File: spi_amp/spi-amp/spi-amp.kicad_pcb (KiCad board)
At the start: 4 copper layers, 5 parts, among them J1 IN+, J2 IN-, J3 OUT+, J4 OUT-, U1 LMH6401

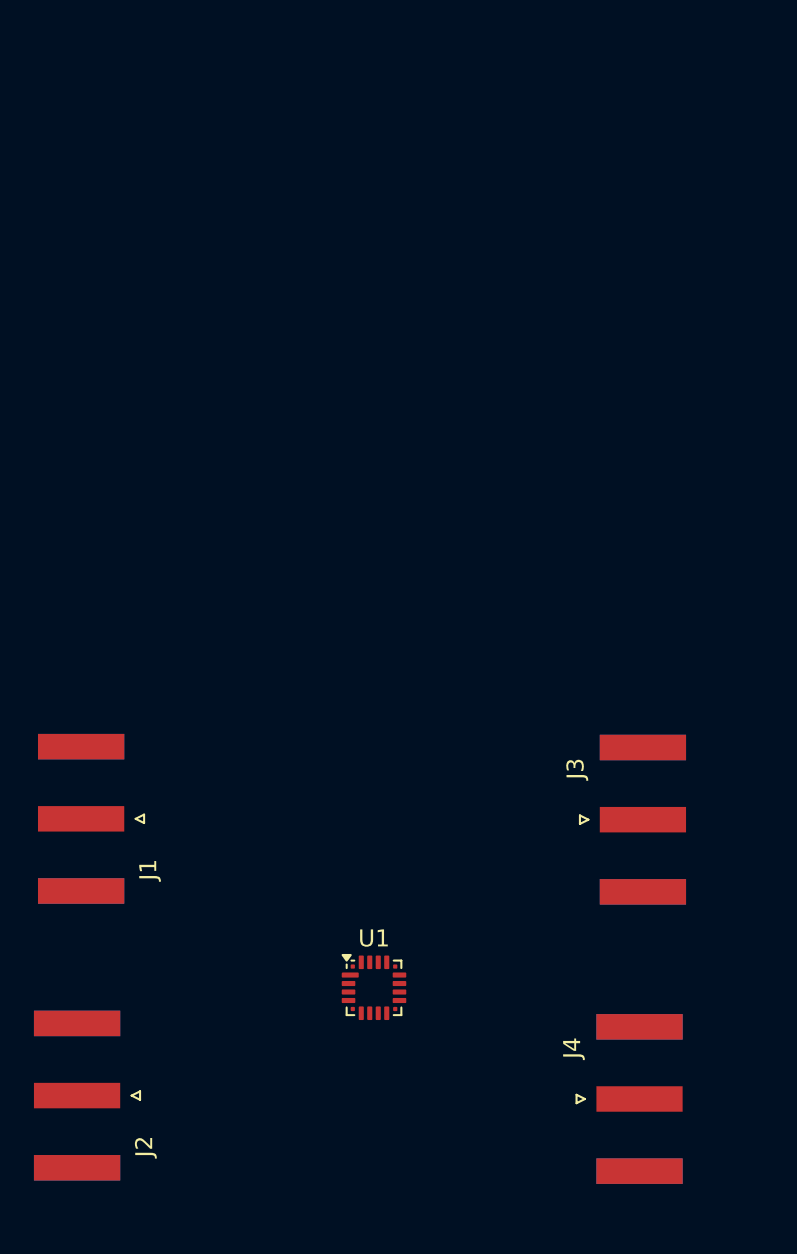
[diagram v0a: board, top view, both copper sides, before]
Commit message: Added SMA connectors with the correct distances.
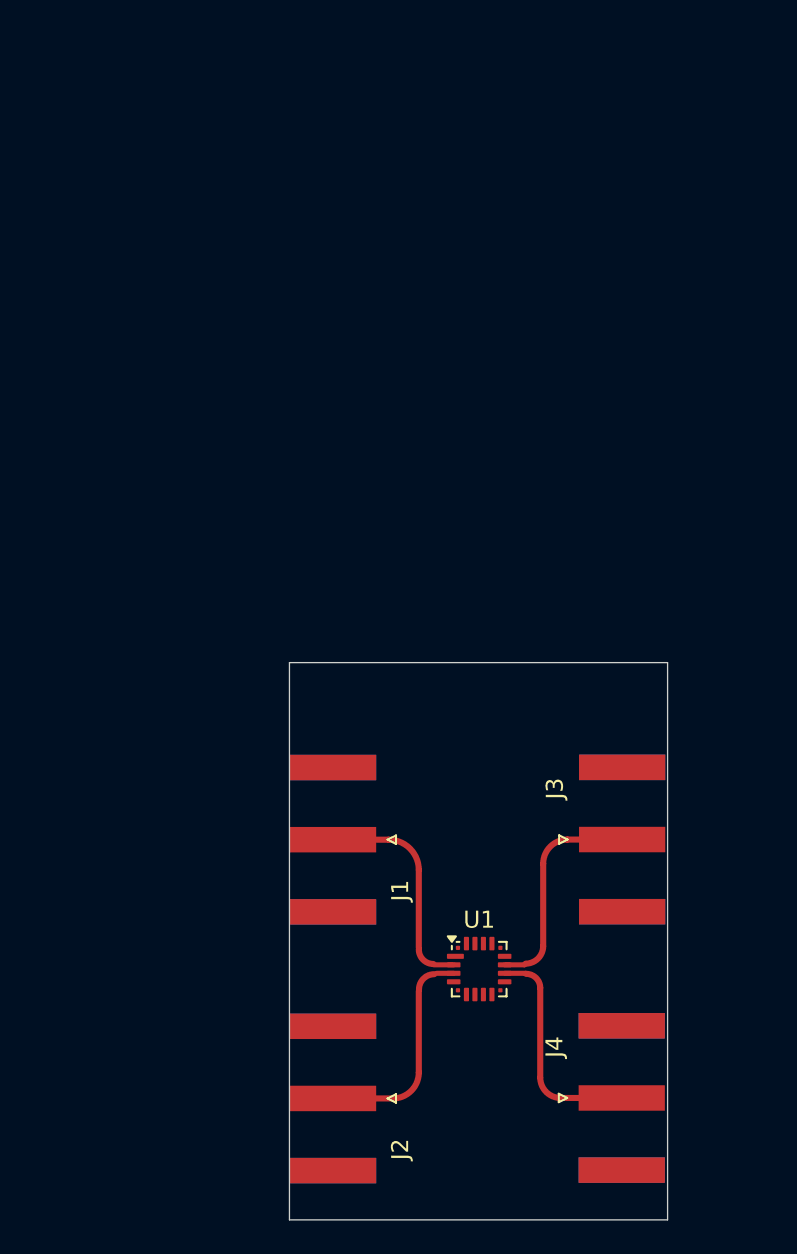
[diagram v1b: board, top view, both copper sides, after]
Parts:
- moved J2 15.1 mm to (108.5, 99.6)
- moved J1 14.9 mm to (108.5, 84.3)
- moved U1 6.29 mm to (117.1, 91.9)
- moved J3 1.69 mm to (125.5, 84.3)
- moved J4 1.05 mm to (125.5, 99.5)
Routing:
- net Net-(J4-In): track 0.00 -> 13.3 mm
- net Net-(J3-In): track 0.00 -> 13.1 mm
- net Net-(J1-In): track 0.00 -> 13.1 mm
- net Net-(J2-In): track 0.00 -> 13.1 mm
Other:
- board outline added: 22.3 x 32.8 mm
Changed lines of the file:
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@@
 	(footprint "Connector_Coaxial:SMA_Amphenol_132289_EdgeMount"
 		(layer "F.Cu")
-		(at 93.65 83.1 180)
+		(at 108.4865 84.328 180)
 		(descr "https://www.amphenolrf.com/library/download/link/link_id/595984/parent/132289/")
 		(tags "SMA")
@@
 	(footprint "Connector_Coaxial:SMA_Amphenol_132289_EdgeMount"
 		(layer "F.Cu")
-		(at 93.4125 99.4 180)
+		(at 108.4865 99.568 180)
 		(descr "https://www.amphenolrf.com/library/download/link/link_id/595984/parent/132289/")
 		(tags "SMA")
@@
 	(footprint "Connector_Coaxial:SMA_Amphenol_132289_EdgeMount"
 		(layer "F.Cu")
-		(at 126.5375 99.6)
+		(at 125.49 99.54)
 		(descr "https://www.amphenolrf.com/library/download/link/link_id/595984/parent/132289/")
 		(tags "SMA")
@@
 	(footprint "Connector_Coaxial:SMA_Amphenol_132289_EdgeMount"
 		(layer "F.Cu")
-		(at 126.7375 83.15)
+		(at 125.514 84.32)
 		(descr "https://www.amphenolrf.com/library/download/link/link_id/595984/parent/132289/")
 		(tags "SMA")
@@
 	(footprint "custom:UQFN-16-custom"
 		(layer "F.Cu")
-		(at 110.9 93.05)
+		(at 117.094 91.948)
 		(descr "16-Lead Ultra Thin Quad Flat, No Lead Package (UC) - 3x3x0.5 mm Body [UQFN]; (see Microchip Packaging Specification 00000049BS.pdf)")
 		(tags "QFN 0.5")
@@
 		)
 	)
+	(gr_rect
+		(start 105.92 73.9)
+		(end 128.19 106.72)
+		(stroke
+			(width 0.05)
+			(type default)
+		)
+		(fill no)
+		(layer "Edge.Cuts")
+	)
+	(segment
+		(start 115.594 91.698)
+		(end 114.411152 91.698)
+		(width 0.3)
+		(layer "F.Cu")
+		(net "Net-(J1-In)")
+	)
+	(segment
+		(start 111.76 84.328)
+		(end 108.4865 84.328)
+		(width 0.36)
+		(layer "F.Cu")
+		(net "Net-(J1-In)")
+	)
+	(segment
+		(start 113.538 86.106)
+		(end 113.538 90.688)
+		(width 0.36)
+		(layer "F.Cu")
+		(net "Net-(J1-In)")
+	)
+	(arc
+		(start 113.538 90.788)
+		(mid 113.790474 91.397526)
+		(end 114.4 91.65)
+		(width 0.36)
+		(layer "F.Cu")
+		(net "Net-(J1-In)")
+	)
+	(arc
+		(start 113.538 86.106)
+		(mid 113.017236 84.848764)
+		(end 111.76 84.328)
+		(width 0.36)
+		(layer "F.Cu")
+		(net "Net-(J1-In)")
+	)
+	(segment
+		(start 113.538 98.044)
+		(end 113.538 93.24419)
+		(width 0.36)
+		(layer "F.Cu")
+		(net "Net-(J2-In)")
+	)
+	(segment
+		(start 115.594 92.198)
+		(end 114.58419 92.198)
+		(width 0.3)
+		(layer "F.Cu")
+		(net "Net-(J2-In)")
+	)
+	(segment
+		(start 108.4865 99.568)
+		(end 112.014 99.568)
+		(width 0.36)
+		(layer "F.Cu")
+		(net "Net-(J2-In)")
+	)
+	(arc
+		(start 113.547905 93.152095)
+		(mid 113.812123 92.514218)
+		(end 114.45 92.25)
+		(width 0.36)
+		(layer "F.Cu")
+		(net "Net-(J2-In)")
+	)
+	(arc
+		(start 112.014 99.568)
+		(mid 113.091631 99.121631)
+		(end 113.538 98.044)
+		(width 0.36)
+		(layer "F.Cu")
+		(net "Net-(J2-In)")
+	)
+	(segment
+		(start 120.69 98.34)
+		(end 120.69 93.06)
+		(width 0.36)
+		(layer "F.Cu")
+		(net "Net-(J4-In)")
+	)
+	(segment
+		(start 125.49 99.54)
+		(end 121.89 99.54)
+		(width 0.36)
+		(layer "F.Cu")
+		(net "Net-(J4-In)")
+	)
+	(segment
+		(start 119.828 92.198)
+		(end 119.86 92.23)
+		(width 0.3)
+		(layer "F.Cu")
+		(net "Net-(J4-In)")
+	)
+	(segment
+		(start 118.594 92.198)
+		(end 119.828 92.198)
+		(width 0.3)
+		(layer "F.Cu")
+		(net "Net-(J4-In)")
+	)
+	(arc
+		(start 120.69 93.06)
+		(mid 120.446899 92.473101)
+		(end 119.86 92.23)
+		(width 0.36)
+		(layer "F.Cu")
+		(net "Net-(J4-In)")
+	)
+	(arc
+		(start 121.89 99.54)
+		(mid 121.041472 99.188528)
+		(end 120.69 98.34)
+		(width 0.36)
+		(layer "F.Cu")
+		(net "Net-(J4-In)")
+	)
+	(segment
+		(start 119.762 91.698)
+		(end 119.83 91.63)
+		(width 0.3)
+		(layer "F.Cu")
+		(net "Net-(J3-In)")
+	)
+	(segment
+		(start 118.594 91.698)
+		(end 119.762 91.698)
+		(width 0.3)
+		(layer "F.Cu")
+		(net "Net-(J3-In)")
+	)
+	(segment
+		(start 125.514 84.32)
+		(end 122.286 84.32)
+		(width 0.36)
+		(layer "F.Cu")
+		(net "Net-(J3-In)")
+	)
+	(segment
+		(start 120.864 85.742)
+		(end 120.864 90.596)
+		(width 0.36)
+		(layer "F.Cu")
+		(net "Net-(J3-In)")
+	)
+	(arc
+		(start 122.286 84.32)
+		(mid 121.280494 84.736494)
+		(end 120.864 85.742)
+		(width 0.36)
+		(layer "F.Cu")
+		(net "Net-(J3-In)")
+	)
+	(arc
+		(start 120.864 90.596)
+		(mid 120.561148 91.327148)
+		(end 119.83 91.63)
+		(width 0.36)
+		(layer "F.Cu")
+		(net "Net-(J3-In)")
+	)
 	(embedded_fonts no)

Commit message: Fixed layout for SPI RF PCB.
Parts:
- added C1: 47n, Capacitor_THT:C_Disc_D4.3mm_W1.9mm_P5.00mm, F.Cu at (130.7, 58.6)
- added C2: 22uF, Capacitor_THT:CP_Radial_D6.3mm_P2.50mm, F.Cu at (127.0, 47.2)
- added C3: 100n, Capacitor_SMD:C_0805_2012Metric_Pad1.18x1.45mm_HandSolder, F.Cu at (124.4, 84.4)
- added C4: 100n, Capacitor_SMD:C_0805_2012Metric_Pad1.18x1.45mm_HandSolder, F.Cu at (124.5, 99.5)
- added C5: 100n, Capacitor_SMD:C_0805_2012Metric_Pad1.18x1.45mm_HandSolder, F.Cu at (116.7, 98.2)
- added C6: 100n, Capacitor_SMD:C_0805_2012Metric_Pad1.18x1.45mm_HandSolder, F.Cu at (116.8, 88.0)
- added C7: 100n, Capacitor_SMD:C_0805_2012Metric_Pad1.18x1.45mm_HandSolder, F.Cu at (116.7, 95.8)
- added J5: Conn_01x02, Connector_PinHeader_2.54mm:PinHeader_1x02_P2.54mm_Vertical, F.Cu at (124.3, 41.7)
- added J6: Conn_01x04, Connector_PinSocket_2.54mm:PinSocket_1x04_P2.54mm_Vertical, F.Cu at (108.9, 45.1)
- added R1: 40, Resistor_SMD:R_0805_2012Metric_Pad1.20x1.40mm_HandSolder, F.Cu at (121.0, 88.2)
- added R10: 1.5k, Resistor_SMD:R_0805_2012Metric_Pad1.20x1.40mm_HandSolder, B.Cu at (124.3, 76.9)
- added R2: 40, Resistor_SMD:R_0805_2012Metric_Pad1.20x1.40mm_HandSolder, F.Cu at (120.8, 95.7)
- added R3: 1k, Resistor_SMD:R_0805_2012Metric_Pad1.20x1.40mm_HandSolder, F.Cu at (115.3, 103.2)
- added R4: 1k, Resistor_SMD:R_0805_2012Metric_Pad1.20x1.40mm_HandSolder, F.Cu at (119.6, 103.2)
- added R5: 1k, Resistor_SMD:R_0805_2012Metric_Pad1.20x1.40mm_HandSolder, B.Cu at (113.9, 52.8)
- added R6: 1k, Resistor_SMD:R_0805_2012Metric_Pad1.20x1.40mm_HandSolder, B.Cu at (116.3, 52.6)
- added R7: 1k, Resistor_SMD:R_0805_2012Metric_Pad1.20x1.40mm_HandSolder, B.Cu at (119.1, 52.6)
- added R8: 1.5k, Resistor_SMD:R_0805_2012Metric_Pad1.20x1.40mm_HandSolder, B.Cu at (114.0, 76.8)
- added R9: 1.5k, Resistor_SMD:R_0805_2012Metric_Pad1.20x1.40mm_HandSolder, B.Cu at (119.2, 76.8)
- added U2: LM78M05_TO220, Package_TO_SOT_THT:TO-220-3_Horizontal_TabDown, F.Cu at (127.0, 58.6)
- added U3: LTV-847S, Package_DIP:SMDIP-16_W9.53mm, B.Cu at (119.1, 68.1)
- moved J3 4.65 mm to (130.2, 84.3)
- moved J4 4.65 mm to (130.1, 99.5)
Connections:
- net Net-(U1-V+-Pad13) renamed VCC
- J1 pad 2: Net-(J1-Ext) -> DIG_GND
- J2 pad 2: Net-(J1-Ext) -> DIG_GND
- J3 pad 2: Net-(J1-Ext) -> DIG_GND
- J4 pad 2: Net-(J1-Ext) -> DIG_GND
- U1 pad 1: unconnected-(U1-SDI-Pad1) -> Net-(U1-SDI)
- U1 pad 10: Net-(J4-In) -> Net-(R2-Pad1)
- U1 pad 11: Net-(J3-In) -> Net-(R1-Pad1)
- U1 pad 12: Net-(J1-Ext) -> DIG_GND
- U1 pad 14: unconnected-(U1-CLK-Pad14) -> Net-(U1-CLK)
- U1 pad 15: unconnected-(U1-CS-Pad15) -> Net-(U1-CS)
- U1 pad 16: Net-(U1-V--Pad16) -> DIG_GND
- U1 pad 17: Net-(J1-Ext) -> DIG_GND
- U1 pad 5: Net-(U1-V--Pad16) -> DIG_GND
- U1 pad 6: unconnected-(U1-PD-Pad6) -> DIG_GND
- U1 pad 7: unconnected-(U1-NC-Pad7) -> Net-(U1-Vocm)
- U1 pad 9: Net-(J1-Ext) -> DIG_GND
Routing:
- net Net-(U1-SDI): track 0.00 -> 28.5 mm, vias 0 -> 1
- net VCC: track 0.00 -> 25.2 mm, vias 0 -> 6
- net Net-(J5-Pin_1): track 0.00 -> 24.9 mm
- net Net-(U1-CS): track 0.00 -> 24.5 mm, vias 0 -> 1
- net Net-(U1-CLK): track 0.00 -> 22.3 mm, vias 0 -> 1
- net DIG_GND: track 0.00 -> 13.1 mm, vias 0 -> 61
- net Net-(U1-Vocm): track 0.00 -> 12.8 mm
- net Net-(R7-Pad1): track 0.00 -> 11.3 mm
- net Net-(R6-Pad1): track 0.00 -> 10.3 mm
- net Net-(R5-Pad1): track 0.00 -> 10.0 mm
- net Net-(J4-In): track 13.3 -> 4.65 mm
- net Net-(J3-In): track 13.1 -> 4.75 mm
- net Net-(J6-Pin_2): track 0.00 -> 7.62 mm
- net Net-(J6-Pin_4): track 0.00 -> 7.57 mm
- net Net-(J6-Pin_3): track 0.00 -> 7.48 mm
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- added copper zone on B.Cu, net DIG_GND
- added copper zone on F.Cu, net DIG_GND
- added copper zone on In1.Cu, net DIG_GND
- added copper zone on B.Cu, net LED_VCC
- added copper zone on In2.Cu, net VCC
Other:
- board size 22.3 x 32.8 mm -> 26.9 x 69.8 mm
- board text added: "0v"
- board text added: "9v"
- board text added: "CLK"
- board text added: "CS"
- board text added: "DIN"
- board text added: "Vcc"

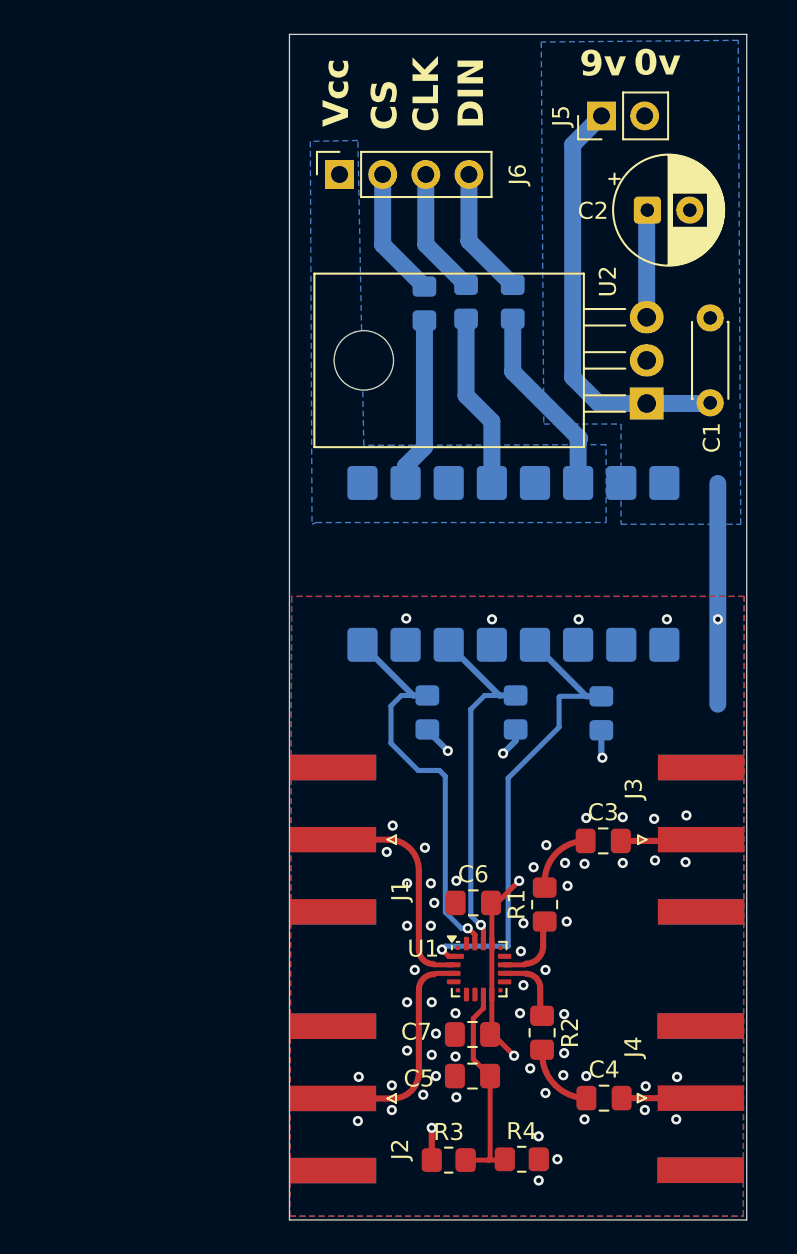
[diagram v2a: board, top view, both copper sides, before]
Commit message: Added inverter on input to handle 3.3v.
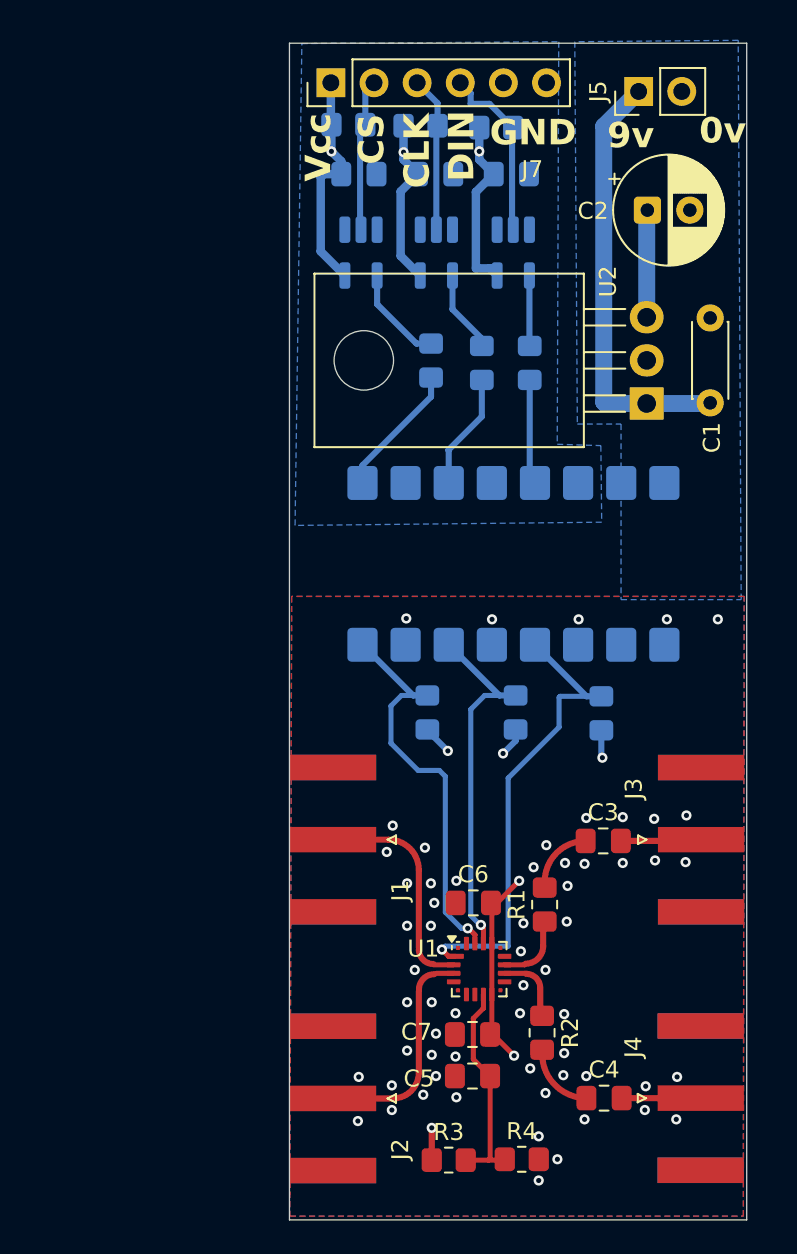
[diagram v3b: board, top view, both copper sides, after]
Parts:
- removed J6: Conn_01x04, Connector_PinSocket_2.54mm:PinSocket_1x04_P2.54mm_Vertical
- added C10: 100n, Capacitor_SMD:C_0805_2012Metric_Pad1.18x1.45mm_HandSolder, B.Cu at (119.0, 45.1)
- added C8: 100n, Capacitor_SMD:C_0805_2012Metric_Pad1.18x1.45mm_HandSolder, B.Cu at (110.0, 45.1)
- added C9: 100n, Capacitor_SMD:C_0805_2012Metric_Pad1.18x1.45mm_HandSolder, B.Cu at (114.5, 45.1)
- added J7: Conn_01x06, Connector_PinHeader_2.54mm:PinHeader_1x06_P2.54mm_Vertical, F.Cu at (108.4, 39.8)
- added R11: 10k, Resistor_SMD:R_0805_2012Metric_Pad1.20x1.40mm_HandSolder, B.Cu at (109.4, 42.2)
- added R12: 10k, Resistor_SMD:R_0805_2012Metric_Pad1.20x1.40mm_HandSolder, B.Cu at (113.6, 42.3)
- added R13: 10k, Resistor_SMD:R_0805_2012Metric_Pad1.20x1.40mm_HandSolder, B.Cu at (118.1, 42.4)
- added U4: 74LVC1G04, Package_TO_SOT_SMD:SOT-23-5_HandSoldering, B.Cu at (110.1, 49.8)
- added U5: 74LVC1G04, Package_TO_SOT_SMD:SOT-23-5_HandSoldering, B.Cu at (114.6, 49.8)
- added U6: 74LVC1G04, Package_TO_SOT_SMD:SOT-23-5_HandSoldering, B.Cu at (119.1, 49.8)
- moved R7 3.74 mm to (120.1, 56.2)
- moved R6 3.72 mm to (117.2, 56.2)
- moved R5 3.38 mm to (114.3, 56.1)
- moved J5 2.62 mm to (126.5, 40.3)
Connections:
- U3 pad 1: LED_VCC -> Net-(R5-Pad1)
- U3 pad 2: Net-(R5-Pad1) -> SPI_GND
- U3 pad 3: LED_VCC -> Net-(R6-Pad1)
- U3 pad 4: Net-(R6-Pad1) -> SPI_GND
- U3 pad 5: LED_VCC -> Net-(R7-Pad1)
- U3 pad 6: Net-(R7-Pad1) -> SPI_GND
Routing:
- net LED_VCC: track 0.00 -> 33.9 mm, vias 0 -> 3
- net DIG_GND: track 13.1 -> 0.14 mm
- net Net-(J7-Pin_4): track 0.00 -> 10.7 mm
- net Net-(J7-Pin_2): track 0.00 -> 9.75 mm
- net Net-(J7-Pin_3): track 0.00 -> 9.18 mm
- net Net-(R7-Pad1): track 11.3 -> 6.20 mm
- net Net-(R6-Pad1): track 10.3 -> 6.89 mm
- net Net-(R7-Pad2): track 7.57 -> 4.21 mm
- net Net-(R6-Pad2): track 7.48 -> 4.86 mm
- net Net-(R5-Pad1): track 10.0 -> 7.88 mm
- net Net-(R5-Pad2): track 7.62 -> 5.83 mm
- net Net-(J5-Pin_1): track 24.9 -> 25.5 mm
- added copper zone on In2.Cu, net LED_VCC
- added copper zone on B.Cu, net SPI_GND
- removed copper zone on B.Cu, net LED_VCC
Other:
- board size 26.9 x 69.8 mm -> 26.9 x 69.3 mm
- board text added: "GND"

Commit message: Added input capacitors.
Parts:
- added C11: 100n, Capacitor_SMD:C_0805_2012Metric_Pad1.18x1.45mm_HandSolder, F.Cu at (113.5, 88.2)
- added C12: 100n, Capacitor_SMD:C_0805_2012Metric_Pad1.18x1.45mm_HandSolder, F.Cu at (113.6, 95.7)
- C1: value 47n -> 470n
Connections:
- U1 pad 2: Net-(J1-In) -> Net-(C11-Pad2)
- U1 pad 3: Net-(J2-In) -> Net-(C12-Pad2)
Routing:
- net Net-(J1-In): track 13.1 -> 7.03 mm
- net Net-(J2-In): track 13.1 -> 7.17 mm
- net Net-(C11-Pad2): track 0.00 -> 4.09 mm
- net Net-(C12-Pad2): track 0.00 -> 3.92 mm
- net DIG_GND: vias 61 -> 119
